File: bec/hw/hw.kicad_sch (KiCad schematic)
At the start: 0 parts

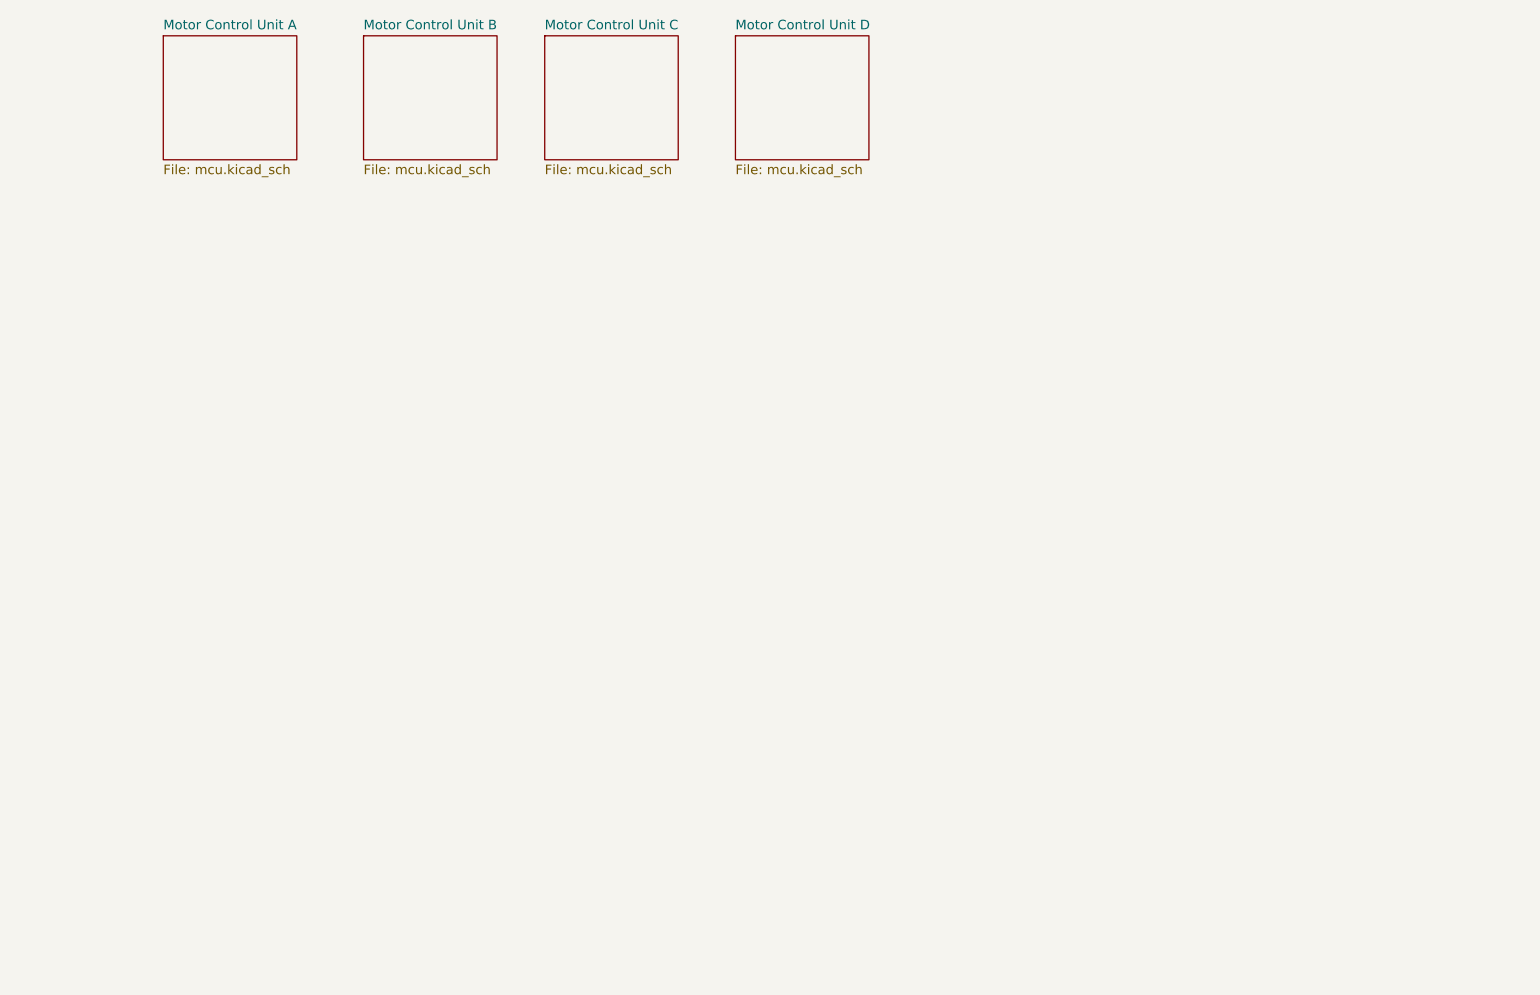
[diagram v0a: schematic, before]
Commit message: Added motor phase half bridges
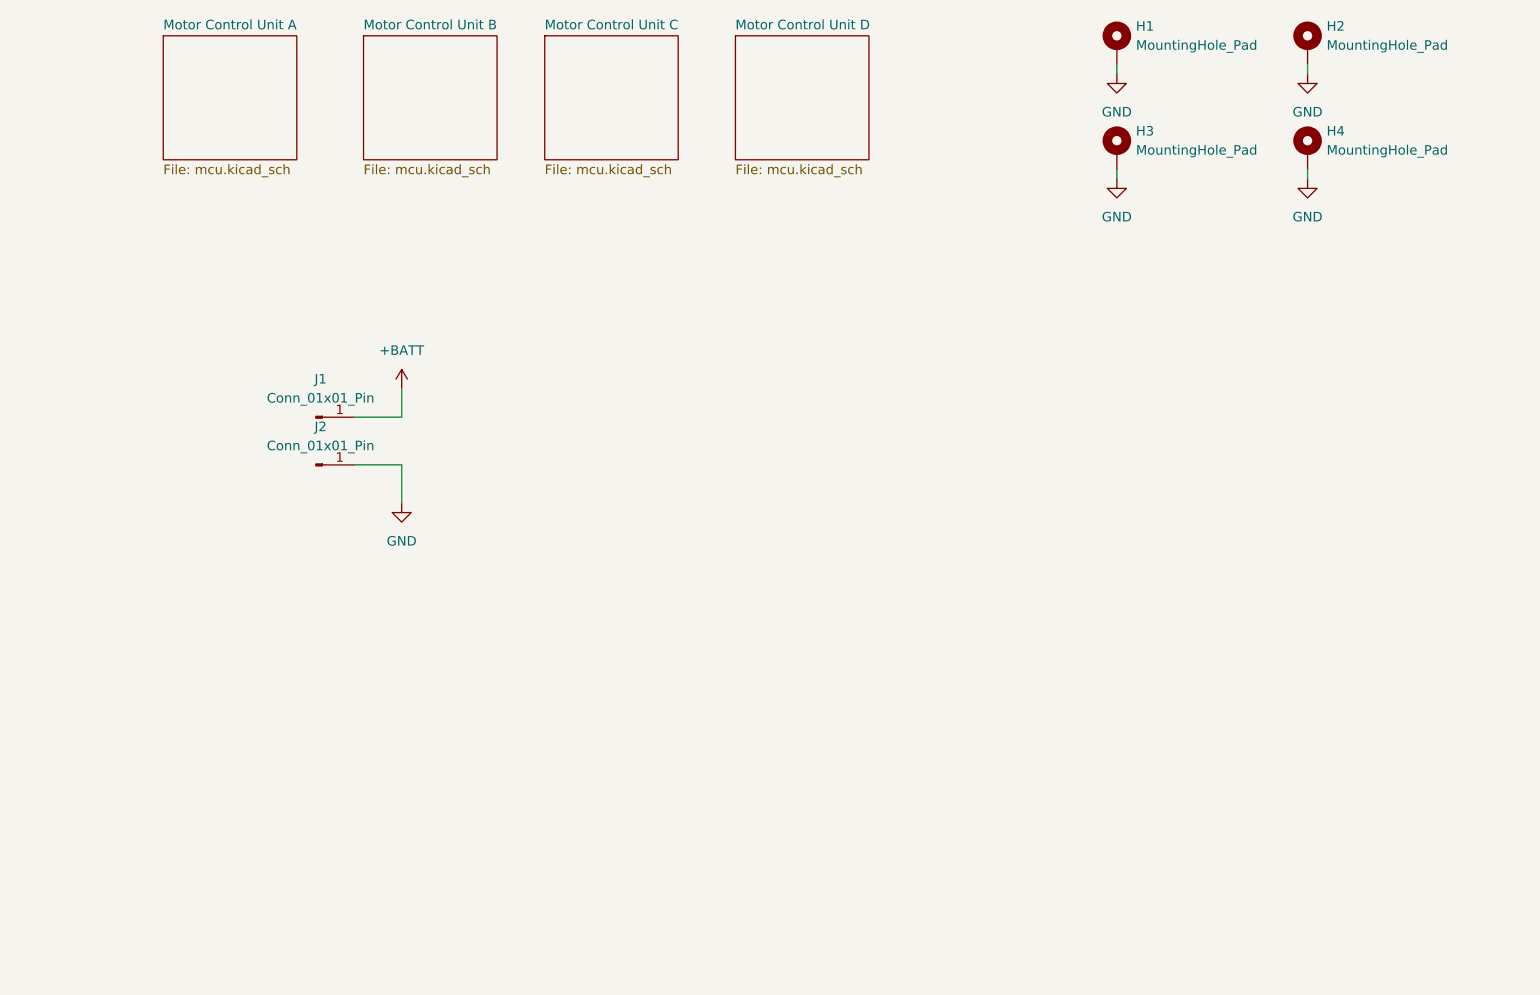
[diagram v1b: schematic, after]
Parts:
- added H1, H2, H3, H4: MountingHole_Pad, MountingHole:MountingHole_4.3mm_M4_DIN965_Pad, symbol Mechanical:MountingHole_Pad
- added J1, J2: Conn_01x01_Pin, CastellatedConnectors:Battery Terminal, symbol Connector:Conn_01x01_Pin
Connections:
- new net +BATT: J1.1 (Pin_1)
- new net GND: H1.1, H2.1, H3.1, H4.1, J2.1 (Pin_1)

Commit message: Added TPS54331 for 3.3v supply
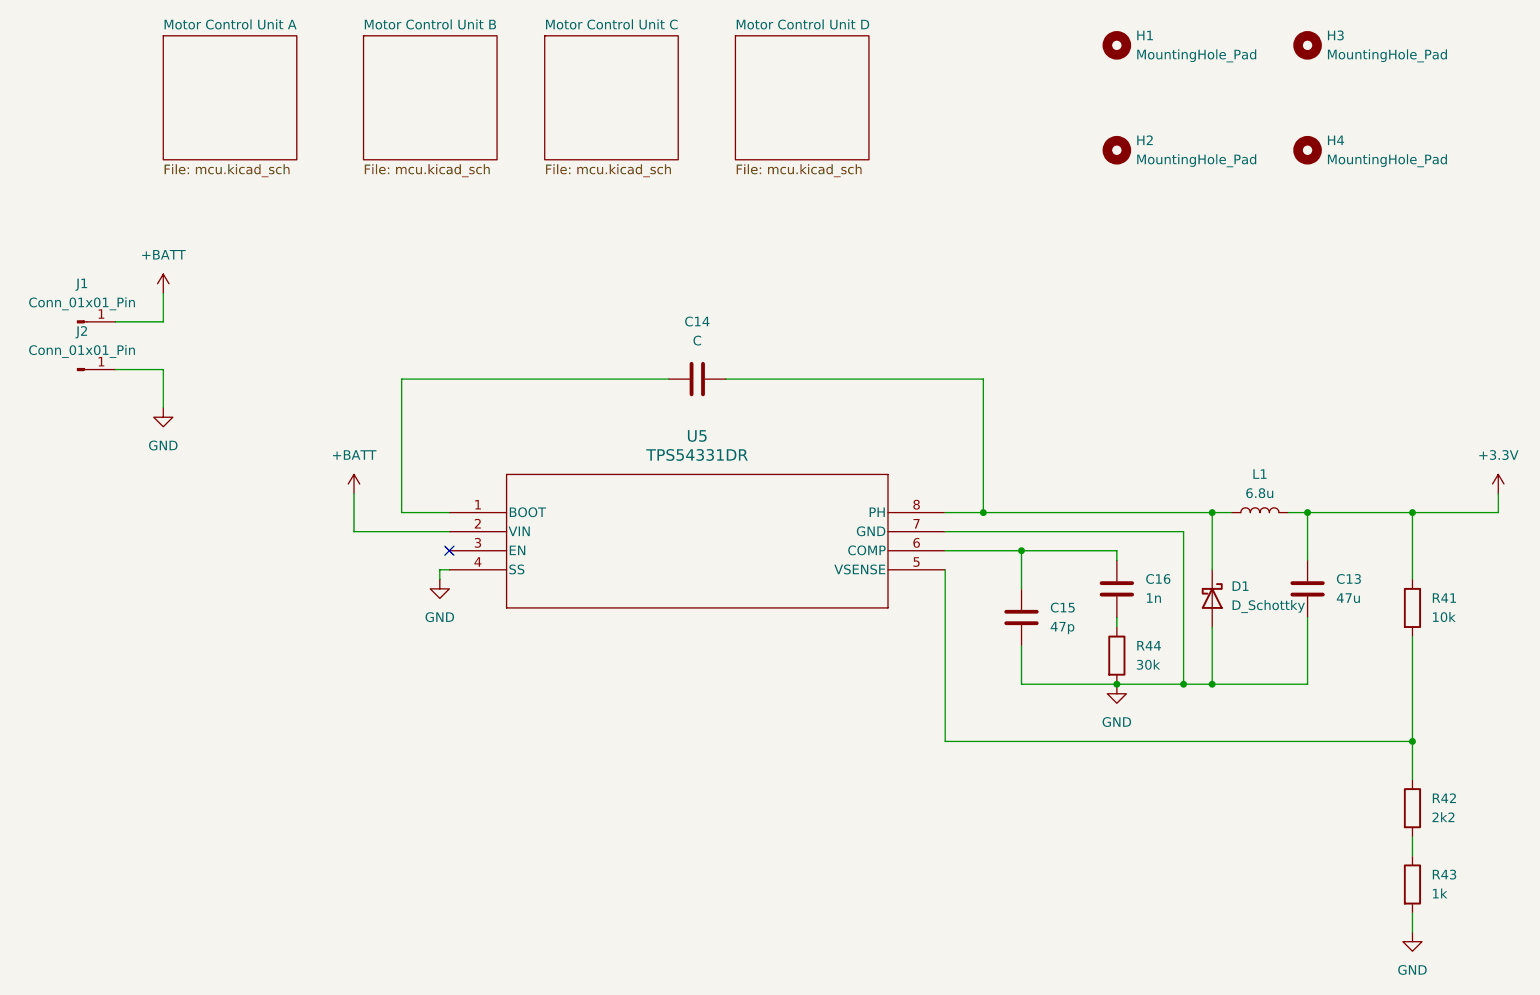
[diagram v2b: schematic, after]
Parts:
- added C13: 47u, Capacitor_SMD:C_0805_2012Metric, symbol Device:C
- added C14: C, Capacitor_SMD:C_0805_2012Metric, symbol Device:C
- added C15: 47p, Capacitor_SMD:C_0805_2012Metric, symbol Device:C
- added C16: 1n, Capacitor_SMD:C_0805_2012Metric, symbol Device:C
- added D1: D_Schottky, symbol Device:D_Schottky
- added L1: 6.8u, symbol Device:L
- added R41: 10k, Resistor_SMD:R_0805_2012Metric, symbol Device:R
- added R42: 2k2, Resistor_SMD:R_0805_2012Metric, symbol Device:R
- added R43: 1k, Resistor_SMD:R_0805_2012Metric, symbol Device:R
- added R44: 30k, Resistor_SMD:R_0805_2012Metric, symbol Device:R
- added U5: TPS54331DR, Snapeda:D8, symbol Snapeda:TPS54331DR
- H1, H4: footprint MountingHole:MountingHole_4.3mm_M4_DIN965_Pad -> MountingHole:MountingHole_4.3mm_M4_DIN965; symbol Mechanical:MountingHole_Pad -> Mechanical:MountingHole
- H2: renamed from H3; footprint MountingHole:MountingHole_4.3mm_M4_DIN965_Pad -> MountingHole:MountingHole_4.3mm_M4_DIN965; symbol Mechanical:MountingHole_Pad -> Mechanical:MountingHole
- H3: renamed from H2; footprint MountingHole:MountingHole_4.3mm_M4_DIN965_Pad -> MountingHole:MountingHole_4.3mm_M4_DIN965; symbol Mechanical:MountingHole_Pad -> Mechanical:MountingHole
- J1, J2: footprint CastellatedConnectors:Battery Terminal -> Connector_Wire:SolderWirePad_1x01_SMD_5x10mm
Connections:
- net +BATT: now also U5.2 (VIN)
- net GND: now also C13.2, C15.1, D1.2 (A), R43.2, R44.2, U5.4 (SS), U5.7 (GND); no longer H1.1, H2.1, H3.1, H4.1
- new net: C14.1, U5.1 (BOOT)
- new net: R41.2, R42.1, U5.5 (VSENSE)
- new net: C15.2, C16.2, U5.6 (COMP)
- new net: C14.2, D1.1 (K), L1.1, U5.8 (PH)
- new net: C16.1, R44.1
- new net: R42.2, R43.1
- new net +3.3V: C13.1, L1.2, R41.1
- no-connect marks 0 -> 1
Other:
- moved on the sheet: J1, J2
